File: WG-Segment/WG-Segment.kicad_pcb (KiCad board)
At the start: 2 copper layers, 100 x 100 mm, 133 parts, among them J101 Conn_01x02, J102 Conn_02x04_Odd_Even, J201 Conn_01x05, J202 Conn_01x02, J203 Conn_01x04, J501 Conn_01x02, J502 Conn_01x02, J503 Conn_01x02, J504 Conn_01x02, J505 Conn_01x02, J506 Conn_01x02, J507 Conn_01x02, J508 Conn_01x02, J509 Conn_01x02, J510 Conn_01x02, J511 Conn_01x02, J512 Conn_01x02, J513 Conn_01x02, J514 Conn_01x02, J515 Conn_01x02, J516 Conn_01x02, J517 Conn_01x02, J518 Conn_01x02, J519 Conn_01x02, J520 Conn_01x02, J521 Conn_01x02, J522 Conn_01x02, J523 Conn_01x02, J524 Conn_01x02, J525 Conn_01x02, SW201 SPST-NO, U201 W25Q16JV, U202 RP2040, U301 AP63205WU, U302 MIC5504-3.3YM5, U303 MCP1501T-33E, U401 SN74LV1T34DCK, U501 SN74LV4051ADYYR, U502 SN74LV4051ADYYR, U503 SN74LV4051ADYYR, U504 SN74LV4051ADYYR, Y201 12MHz

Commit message: Add 5x5 LED grid to PCB
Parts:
- D401, D402, D403, D404, D405, D406, D407, D408, D409, D410, D411, D412, D413, D414, D415, D416, D417, D418, D419, D420, D421, D422, D423, D424, D425, J501, J502, J503, J504, J505, J506, J507, J508, J509, J510, J511, J512, J513, J514, J515, J516, J517, J518, J519, J520, J521, J522, J523, J524, J525: moved to B.Cu
- moved J521 269.6 mm to (107.7, 145.1), turned to 180 degrees
- moved J520 265.7 mm to (107.7, 125.1), turned to 180 degrees
- moved J510 263.1 mm to (107.7, 85.1), turned to 180 degrees
- moved J511 262.0 mm to (107.7, 105.1), turned to 180 degrees
- moved J501 260.7 mm to (107.7, 65.1), turned to 180 degrees
- moved J522 249.5 mm to (127.7, 145.1), turned to 180 degrees
- moved D421 246.5 mm to (107.2, 138.1), turned to 180 degrees
- moved J519 245.5 mm to (127.7, 125.1), turned to 180 degrees
- moved J509 242.9 mm to (127.7, 85.1), turned to 180 degrees
- moved J512 242.5 mm to (127.7, 105.1), turned to 180 degrees
- moved J502 242.3 mm to (127.7, 65.1), turned to 180 degrees
- moved D420 236.6 mm to (107.2, 118.1)
- moved J523 229.4 mm to (147.7, 145.1), turned to 180 degrees
- moved D411 227.8 mm to (107.2, 98.1), turned to 180 degrees
- moved D410 226.1 mm to (107.2, 78.1)
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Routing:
- net /LED/ROW2_3: track 0.00 -> 20.9 mm
- net /LED/ROW4_5: track 0.00 -> 20.9 mm
- net /LED/ROW3_4: track 0.00 -> 20.9 mm
- net Net-(D421-DOUT): track 0.00 -> 16.5 mm
- net Net-(D424-DOUT): track 0.00 -> 16.5 mm
- net Net-(D423-DOUT): track 0.00 -> 16.5 mm
- net Net-(D422-DOUT): track 0.00 -> 16.5 mm
- net Net-(D418-DOUT): track 0.00 -> 16.5 mm
- net Net-(D417-DOUT): track 0.00 -> 16.5 mm
- net Net-(D416-DOUT): track 0.00 -> 16.5 mm
- net Net-(D408-DOUT): track 0.00 -> 16.5 mm
- net Net-(D407-DOUT): track 0.00 -> 16.5 mm
- net Net-(D406-DOUT): track 0.00 -> 16.5 mm
- net Net-(D401-DOUT): track 0.00 -> 16.5 mm
- net Net-(D419-DOUT): track 0.00 -> 16.5 mm
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
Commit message: Position power circuitry
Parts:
- moved C426 249.2 mm to (112.7, 35.4)
- moved U401 246.9 mm to (113.6, 38.8)
- moved R203 33.4 mm to (347.9, 91.3), turned to 90 degrees
- moved R202 32.2 mm to (346.8, 91.3), turned to 90 degrees
- moved U202 31.5 mm to (346.1, 101.0)
- moved U302 31.2 mm to (376.6, 164.7), turned to -90 degrees
- moved C306 30.3 mm to (378.8, 166.0), turned to 90 degrees
- moved C305 30.3 mm to (378.8, 163.4), turned to -90 degrees
- moved J201 27.5 mm to (351.2, 85.7), turned to -90 degrees
- moved C206 24.7 mm to (340.7, 98.4), turned to 180 degrees
- moved C302 23.1 mm to (327.3, 176.4)
- moved C301 22.6 mm to (328.6, 171.1)
- moved C205 21.5 mm to (340.7, 102.0), turned to 180 degrees
- moved C208 20.3 mm to (345.6, 95.6), turned to 90 degrees
- moved C207 18.4 mm to (346.6, 95.6), turned to 90 degrees
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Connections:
- net Net-(U202-VREG_VOUT) renamed +1V1
- net Net-(U301-SW) renamed /Power/SW
- C204 pad 1: +3.3V -> +3V3
- C205 pad 1: +3.3V -> +3V3
- C206 pad 1: +3.3V -> +3V3
- C207 pad 1: +3.3V -> +3V3
- C208 pad 1: +3.3V -> +3V3
- C209 pad 1: +3.3V -> +3V3
- C210 pad 1: +3.3V -> +3V3
- C211 pad 1: +3.3V -> +3V3
- C213 pad 1: +3.3V -> +3V3
- J203 pad 1: +3.3V -> +3V3
- R201 pad 1: +3.3V -> +3V3
- R204 pad 1: +3.3V -> +3V3
- U201 pad 8: +3.3V -> +3V3
- U202 pad 1: +3.3V -> +3V3
- U202 pad 10: +3.3V -> +3V3
- U202 pad 22: +3.3V -> +3V3
- U202 pad 33: +3.3V -> +3V3
- U202 pad 42: +3.3V -> +3V3
- U202 pad 44: +3.3V -> +3V3
- U202 pad 48: +3.3V -> +3V3
- U202 pad 49: +3.3V -> +3V3
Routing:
- added copper zone on F.Cu, net +12V
- added copper zone on F.Cu, net +3V3
- added copper zone on F.Cu, net +5V
- added copper zone on F.Cu, net /Power/SW
- added copper zone on F.Cu, net GND

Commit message: Finish designing most of the PCB
Only need to connect analog traces. May need to make the board a 4-layer PCB
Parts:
- J201: value Conn_01x05 -> Conn_01x03; footprint Connector_PinSocket_2.54mm:PinSocket_1x05_P2.54mm_Vertical -> Connector_PinHeader_2.54mm:PinHeader_1x03_P2.54mm_Vertical
- moved R501 264.5 mm to (116.8, 125.5)
- moved R504 254.9 mm to (136.9, 65.3)
- moved U504 254.8 mm to (137.2, 68.1), turned to -90 degrees
- moved J202 249.2 mm to (127.5, 88.7), turned to -90 degrees
- moved U501 247.4 mm to (117.1, 128.3), turned to -90 degrees
- moved U201 246.8 mm to (132.3, 85.9), turned to 90 degrees
- moved Y201 243.4 mm to (137.2, 102.4), turned to -90 degrees
- moved C501 240.3 mm to (119.9, 128.9), turned to 90 degrees
- moved R205 238.5 mm to (128.0, 91.0), turned to 180 degrees
- moved C306 238.2 mm to (153.7, 88.1), turned to 0 degrees
- moved C213 238.1 mm to (128.8, 82.4), turned to 90 degrees
- moved C302 237.4 mm to (114.0, 72.1)
- moved C303 237.4 mm to (121.7, 72.1)
- moved C304 237.4 mm to (117.9, 72.1)
- moved L301 237.4 mm to (119.6, 68.1)
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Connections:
- J102 pad 7: /SDA -> /SCK
- J102 pad 8: /SCK -> /SDA
- J201 pad 1: unconnected-(J201-Pin_1-Pad1) -> /CPU/USB_D-
- J201 pad 2: /CPU/USB_D- -> /CPU/USB_D+
- J201 pad 3: /CPU/USB_D+ -> GND
- U202 pad 12: unconnected-(U202-GPIO9-Pad12) -> /CPU/MUX_C
- U202 pad 13: unconnected-(U202-GPIO10-Pad13) -> /CPU/MUX_B
- U202 pad 14: unconnected-(U202-GPIO11-Pad14) -> /CPU/MUX_A
- U202 pad 2: /SDA -> unconnected-(U202-GPIO0-Pad2)
- U202 pad 3: /SCK -> unconnected-(U202-GPIO1-Pad3)
- U202 pad 30: /CPU/MUX_A -> unconnected-(U202-GPIO19-Pad30)
- U202 pad 31: /CPU/MUX_B -> unconnected-(U202-GPIO20-Pad31)
- U202 pad 32: /CPU/MUX_C -> unconnected-(U202-GPIO21-Pad32)
- U202 pad 4: /~{DS}/~{INT} -> unconnected-(U202-GPIO2-Pad4)
- U202 pad 5: unconnected-(U202-GPIO3-Pad5) -> /CPU/LED_DOUT
- U202 pad 6: /CPU/LED_DOUT -> unconnected-(U202-GPIO4-Pad6)
- U202 pad 7: unconnected-(U202-GPIO5-Pad7) -> /~{DS}/~{INT}
- U202 pad 8: unconnected-(U202-GPIO6-Pad8) -> /SDA
- U202 pad 9: unconnected-(U202-GPIO7-Pad9) -> /SCK
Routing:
- net +5V: track 0.00 -> 997.2 mm, vias 0 -> 49
- net /CPU/MUX_C: track 0.00 -> 212.4 mm
- net /CPU/MUX_B: track 0.00 -> 211.3 mm, vias 0 -> 2
- net /CPU/MUX_A: track 0.00 -> 210.0 mm, vias 0 -> 2
- net /CPU/MUX_~{EN}_4: track 0.00 -> 77.0 mm
- net /CPU/MUX_~{EN}_1: track 0.00 -> 62.7 mm
- net /CPU/LED_DOUT: track 0.00 -> 58.6 mm
- net /CPU/MUX_~{EN}_2: track 0.00 -> 52.9 mm, vias 0 -> 2
- net +3V3: track 0.00 -> 48.9 mm
- net /CPU/MUX_~{EN}_3: track 0.00 -> 37.2 mm, vias 0 -> 2
- net GND: track 0.00 -> 34.1 mm, vias 0 -> 39
- net +1V1: track 0.00 -> 24.2 mm
- net /~{DS}/~{INT}: track 0.00 -> 22.9 mm
- net /SCK: track 0.00 -> 22.1 mm
- net +12V: track 0.00 -> 21.4 mm
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- added copper zone on B.Cu, net +5V
- added copper zone on B.Cu, net GND

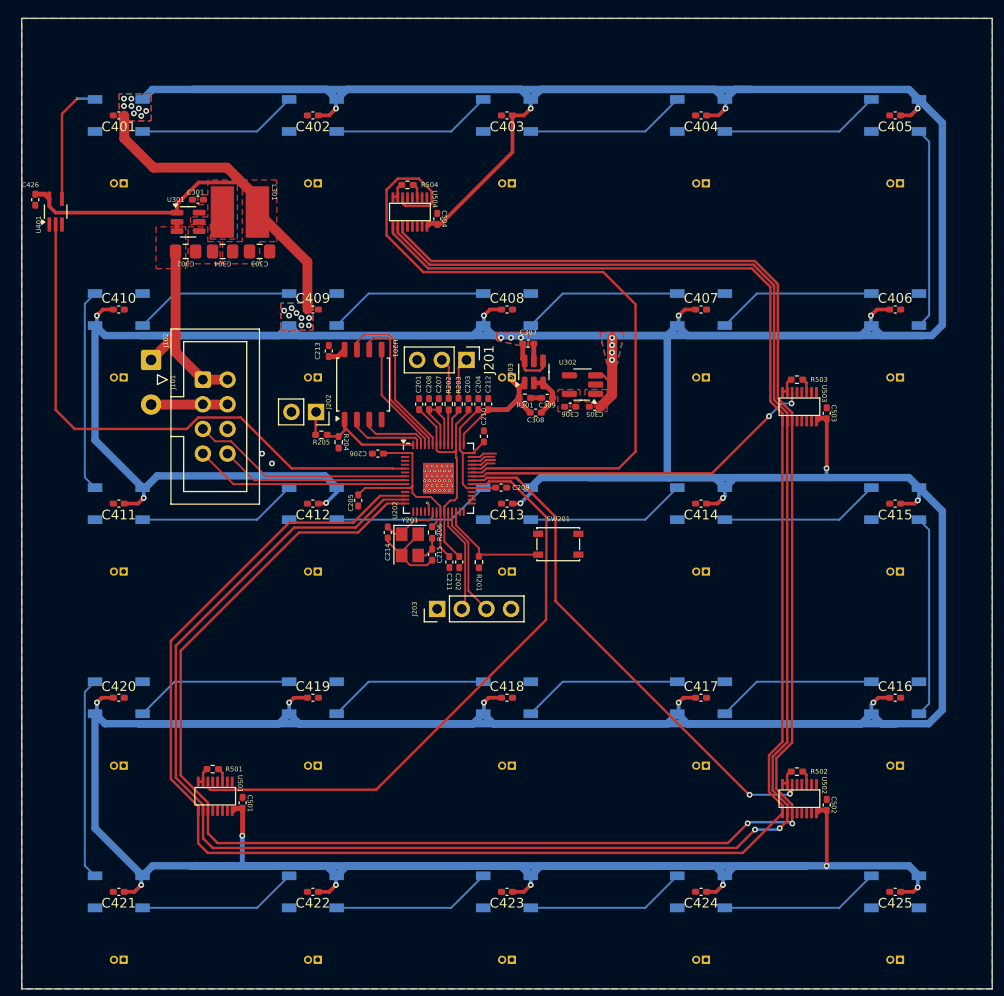
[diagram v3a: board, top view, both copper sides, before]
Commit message: Change PCB to 4 layers
Also fix all errors
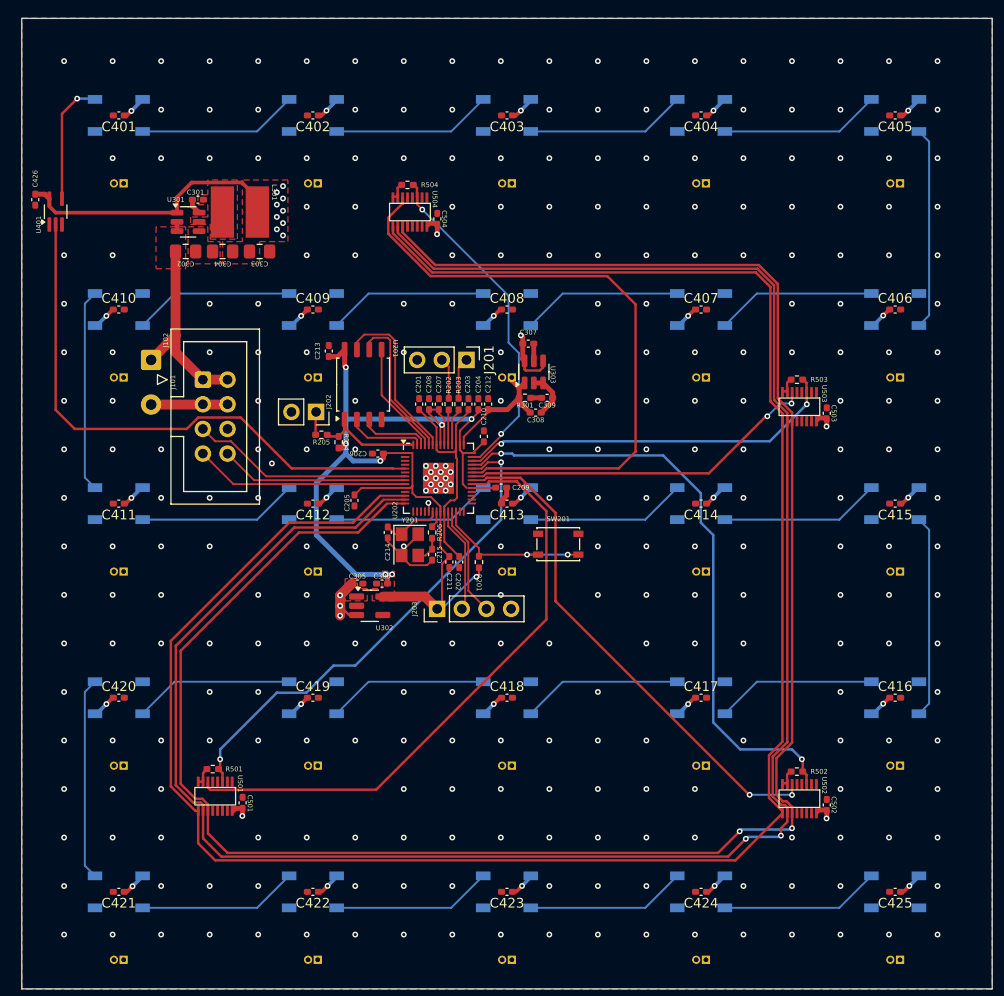
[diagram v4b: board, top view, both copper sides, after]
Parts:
- moved U302 31.6 mm to (133.0, 108.6), turned to 0 degrees
- moved C305 30.5 mm to (131.7, 106.4), turned to 0 degrees
- moved C306 26.6 mm to (134.3, 106.4), turned to 180 degrees
- moved C205 0.38 mm to (131.4, 97.8)
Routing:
- net +5V: track 997.2 -> 102.1 mm, vias 49 -> 42
- net VREF: track 13.6 -> 499.4 mm
- net +3V3: track 48.9 -> 115.6 mm, vias 0 -> 8
- net /CPU/ADC1: track 4.07 -> 63.4 mm, vias 0 -> 2
- net /CPU/ADC0: track 4.04 -> 51.3 mm, vias 0 -> 2
- net /CPU/ADC2: track 3.96 -> 39.6 mm, vias 0 -> 2
- net /CPU/ADC3: track 4.12 -> 35.0 mm, vias 0 -> 2
- net /CPU/MUX_~{EN}_4: track 77.0 -> 66.4 mm
- net Net-(U202-RUN): track 11.7 -> 16.8 mm, vias 0 -> 2
- net /CPU/MUX_B: track 211.3 -> 213.2 mm
- net Net-(U301-BST): track 0.00 -> 1.62 mm
- net /CPU/MUX_A: track 210.0 -> 211.6 mm
- net /CPU/MUX_C: track 212.4 -> 213.2 mm
- net /CPU/FLASH_SD3: track 17.7 -> 16.9 mm
- net GND: track 34.1 -> 33.8 mm, vias 39 -> 289
- added copper zone on In2.Cu, net +5V
- added copper zone on In1.Cu, net GND
- removed copper zone on B.Cu, net +5V
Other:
- copper layers 2 -> 4
- board text added: "TODO: - add 5V bridges over VREF lines in copper plane - connect analog header inputs to MUXes"

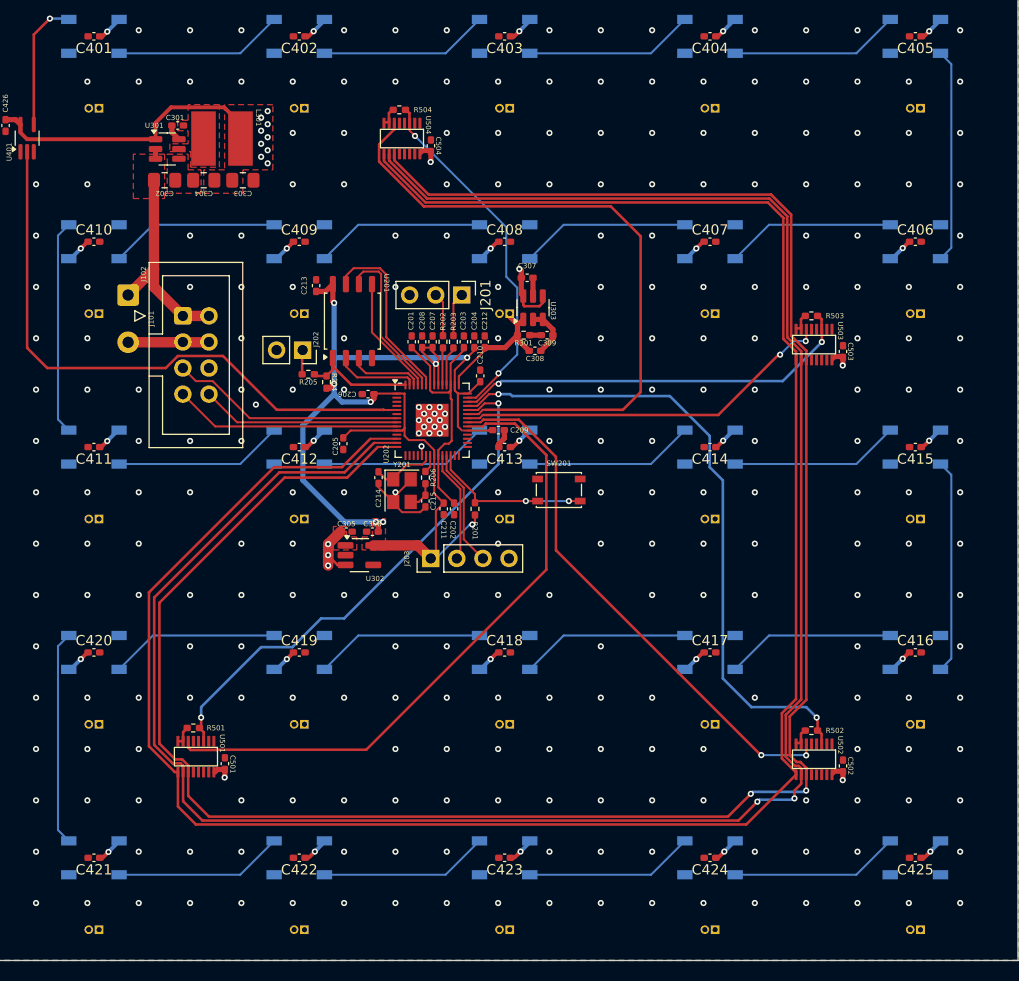
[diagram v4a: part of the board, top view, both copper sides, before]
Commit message: Add ADC-tile connections
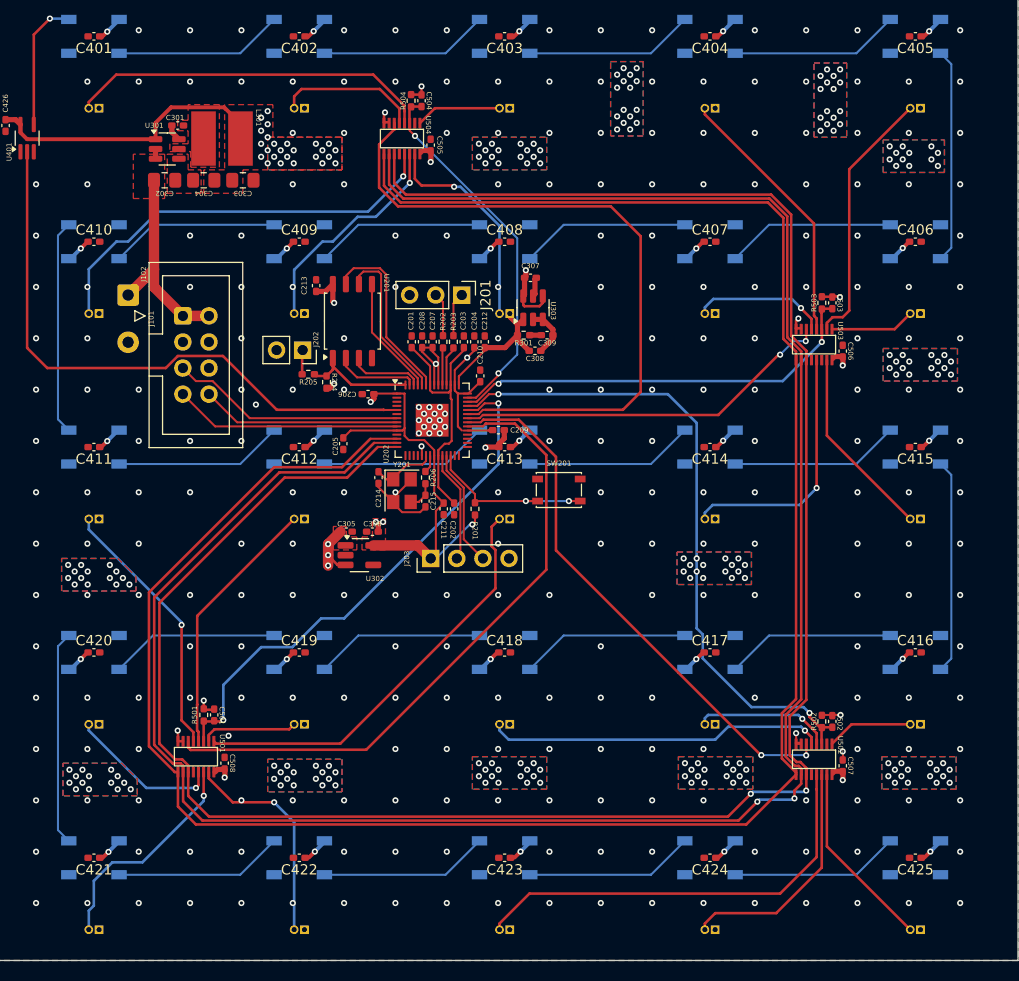
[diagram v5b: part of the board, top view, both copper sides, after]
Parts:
- added C505: 0.1u, Capacitor_SMD:C_0402_1005Metric_Pad0.74x0.62mm_HandSolder, F.Cu at (140.0, 68.7)
- added C506: 0.1u, Capacitor_SMD:C_0402_1005Metric_Pad0.74x0.62mm_HandSolder, F.Cu at (180.1, 88.8)
- added C507: 0.1u, Capacitor_SMD:C_0402_1005Metric_Pad0.74x0.62mm_HandSolder, F.Cu at (180.1, 129.2)
- added C508: 0.1u, Capacitor_SMD:C_0402_1005Metric_Pad0.74x0.62mm_HandSolder, F.Cu at (119.9, 128.9)
- C501, C502, C503, C504: value 0.1u -> 100n
- moved C501 4.86 mm to (118.9, 124.2)
- moved C503 4.85 mm to (179.1, 84.1)
- moved C504 4.48 mm to (139.1, 64.4)
- moved C502 4.45 mm to (179.1, 124.8)
- moved R501 1.63 mm to (117.9, 124.2), turned to -90 degrees
- moved R503 1.63 mm to (178.1, 84.1), turned to -90 degrees
- moved R504 1.45 mm to (138.0, 64.4), turned to -90 degrees
- moved R502 1.35 mm to (178.1, 124.8), turned to -90 degrees
- moved C307 0.32 mm to (149.7, 81.6)
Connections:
- C501 pad 1: +5V -> /CPU/ADC0
- C502 pad 1: +5V -> /CPU/ADC1
- C503 pad 1: +5V -> /CPU/ADC2
- C504 pad 1: +5V -> /CPU/ADC3
- J501 pad 2: unconnected-(J501-Pin_2-Pad2) -> /Tile Connector/A1
- J502 pad 2: unconnected-(J502-Pin_2-Pad2) -> /Tile Connector/A2
- J503 pad 2: unconnected-(J503-Pin_2-Pad2) -> /Tile Connector/A3
- J504 pad 2: unconnected-(J504-Pin_2-Pad2) -> /Tile Connector/A4
- J505 pad 2: unconnected-(J505-Pin_2-Pad2) -> /Tile Connector/A5
- J506 pad 2: unconnected-(J506-Pin_2-Pad2) -> /Tile Connector/A6
- J507 pad 2: unconnected-(J507-Pin_2-Pad2) -> /Tile Connector/A7
- J508 pad 2: unconnected-(J508-Pin_2-Pad2) -> /Tile Connector/A8
- J509 pad 2: unconnected-(J509-Pin_2-Pad2) -> /Tile Connector/A9
- J510 pad 2: unconnected-(J510-Pin_2-Pad2) -> /Tile Connector/A10
- J511 pad 2: unconnected-(J511-Pin_2-Pad2) -> /Tile Connector/A11
- J512 pad 2: unconnected-(J512-Pin_2-Pad2) -> /Tile Connector/A12
- J513 pad 2: unconnected-(J513-Pin_2-Pad2) -> /Tile Connector/A13
- J514 pad 2: unconnected-(J514-Pin_2-Pad2) -> /Tile Connector/A14
- J515 pad 2: unconnected-(J515-Pin_2-Pad2) -> /Tile Connector/A15
- J516 pad 2: unconnected-(J516-Pin_2-Pad2) -> /Tile Connector/A16
- J517 pad 2: unconnected-(J517-Pin_2-Pad2) -> /Tile Connector/A17
- J518 pad 2: unconnected-(J518-Pin_2-Pad2) -> /Tile Connector/A18
- J519 pad 2: unconnected-(J519-Pin_2-Pad2) -> /Tile Connector/A19
- J520 pad 2: unconnected-(J520-Pin_2-Pad2) -> /Tile Connector/A20
- J521 pad 2: unconnected-(J521-Pin_2-Pad2) -> /Tile Connector/A21
- J522 pad 2: unconnected-(J522-Pin_2-Pad2) -> /Tile Connector/A22
- J523 pad 2: unconnected-(J523-Pin_2-Pad2) -> /Tile Connector/A23
- J524 pad 2: unconnected-(J524-Pin_2-Pad2) -> /Tile Connector/A24
- J525 pad 2: unconnected-(J525-Pin_2-Pad2) -> /Tile Connector/A25
- U501 pad 1: unconnected-(U501-Y4-Pad1) -> /Tile Connector/A13
- U501 pad 13: unconnected-(U501-Y0-Pad13) -> /Tile Connector/A20
- U501 pad 14: unconnected-(U501-Y1-Pad14) -> /Tile Connector/A21
- U501 pad 15: unconnected-(U501-Y2-Pad15) -> /Tile Connector/A22
- U501 pad 2: unconnected-(U501-Y6-Pad2) -> /Tile Connector/A19
- U501 pad 4: unconnected-(U501-Y7-Pad4) -> /Tile Connector/A12
- U501 pad 5: unconnected-(U501-Y5-Pad5) -> /Tile Connector/A11
- U502 pad 1: unconnected-(U502-Y4-Pad1) -> /Tile Connector/A16
- U502 pad 13: unconnected-(U502-Y0-Pad13) -> /Tile Connector/A23
- U502 pad 14: unconnected-(U502-Y1-Pad14) -> /Tile Connector/A24
- U502 pad 15: unconnected-(U502-Y2-Pad15) -> /Tile Connector/A25
- U502 pad 4: unconnected-(U502-Y7-Pad4) -> /Tile Connector/A17
- U502 pad 5: unconnected-(U502-Y5-Pad5) -> /Tile Connector/A18
- U503 pad 1: unconnected-(U503-Y4-Pad1) -> /Tile Connector/A6
- U503 pad 13: unconnected-(U503-Y0-Pad13) -> /Tile Connector/A14
- U503 pad 15: unconnected-(U503-Y2-Pad15) -> /Tile Connector/A15
- U503 pad 2: unconnected-(U503-Y6-Pad2) -> /Tile Connector/A5
- U503 pad 4: unconnected-(U503-Y7-Pad4) -> /Tile Connector/A4
- U503 pad 5: unconnected-(U503-Y5-Pad5) -> /Tile Connector/A7
- U504 pad 1: unconnected-(U504-Y4-Pad1) -> /Tile Connector/A3
- U504 pad 13: unconnected-(U504-Y0-Pad13) -> /Tile Connector/A10
- U504 pad 14: unconnected-(U504-Y1-Pad14) -> /Tile Connector/A9
- U504 pad 15: unconnected-(U504-Y2-Pad15) -> /Tile Connector/A8
- U504 pad 4: unconnected-(U504-Y7-Pad4) -> /Tile Connector/A1
- U504 pad 5: unconnected-(U504-Y5-Pad5) -> /Tile Connector/A2
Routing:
- net VREF: track 499.4 -> 739.3 mm
- net /Tile Connector/A23: track 0.00 -> 42.2 mm
- net /Tile Connector/A13: track 0.00 -> 41.0 mm
- net /Tile Connector/A10: track 0.00 -> 40.9 mm, vias 0 -> 1
- net /Tile Connector/A1: track 0.00 -> 35.4 mm
- net /Tile Connector/A18: track 0.00 -> 33.0 mm, vias 0 -> 1
- net /Tile Connector/A4: track 0.00 -> 26.0 mm
- net /Tile Connector/A11: track 0.00 -> 25.9 mm, vias 0 -> 1
- net /Tile Connector/A12: track 0.00 -> 25.6 mm
- net /Tile Connector/A5: track 0.00 -> 25.5 mm
- net /Tile Connector/A14: track 0.00 -> 25.0 mm, vias 0 -> 1
- net /Tile Connector/A24: track 0.00 -> 23.3 mm
- net /Tile Connector/A9: track 0.00 -> 21.9 mm, vias 0 -> 1
- net /Tile Connector/A21: track 0.00 -> 21.7 mm, vias 0 -> 1
- net /Tile Connector/A22: track 0.00 -> 21.2 mm, vias 0 -> 1
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- added copper zone on B.Cu, net +5V

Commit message: Fix DRC errors
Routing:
- net GND: track 34.6 -> 33.3 mm, vias 299 -> 359
- net /CPU/ADC1: vias 4 -> 2
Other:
- board text removed: "TODO: - add 5V bridges over VREF lines in copper plane - connect analog header inputs to MUXes"

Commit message: Update connector
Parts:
- J102: footprint Connector_IDC:IDC-Header_2x04_P2.54mm_Vertical -> Connector_JST:JST_PHD_B8B-PHDSS_2x04_P2.00mm_Vertical
- moved J102 2.30 mm to (118.1, 85.3), turned to -90 degrees
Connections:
- J102 pad 5: /~{DS}/~{INT} -> GND
- J102 pad 6: GND -> /~{DS}/~{INT}
- J102 pad 7: /SCK -> /SDA
- J102 pad 8: /SDA -> /SCK
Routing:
- net /SDA: track 19.4 -> 21.2 mm
- net /SCK: track 22.1 -> 23.6 mm
- net /~{DS}/~{INT}: track 22.9 -> 23.7 mm
- net /CPU/LED_DOUT: track 58.6 -> 59.3 mm
- net GND: vias 359 -> 358
